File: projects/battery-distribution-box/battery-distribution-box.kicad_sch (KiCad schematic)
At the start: 6 parts, among them J1 Cells, J2 Diag, J3 Balancer, J4 Output, J5 Balancer enable

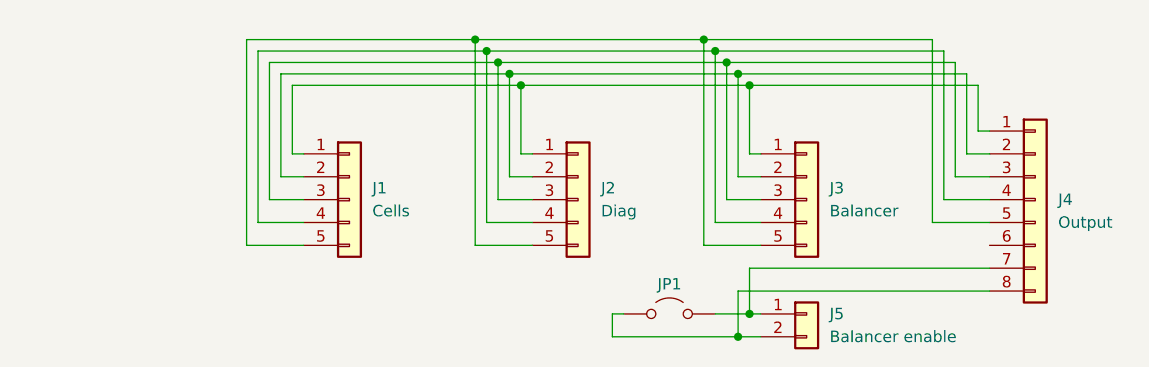
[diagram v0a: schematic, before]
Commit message: Moving to JST VH connectors. They are cheaper and easier to source.
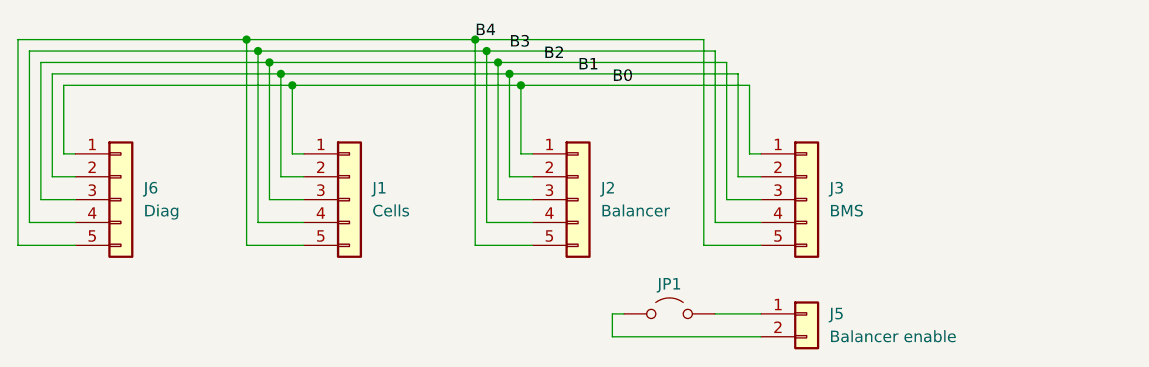
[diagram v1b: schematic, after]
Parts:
- removed J4: Output, Connector_RJ:RJ45_OST_PJ012-8P8CX_Vertical, symbol Connector_Generic:Conn_01x08
- added J6: Diag, Connector_JST:JST_VH_B5PS-VH_1x05_P3.96mm_Horizontal, symbol Connector_Generic:Conn_01x05
- J1: footprint Connector_Phoenix_MC:PhoenixContact_MCV_1,5_5-G-3.5_1x05_P3.50mm_Vertical -> Connector_JST:JST_VH_B5PS-VH_1x05_P3.96mm_Horizontal
- J2: value Diag -> Balancer; footprint Connector_Phoenix_MC:PhoenixContact_MCV_1,5_5-G-3.5_1x05_P3.50mm_Vertical -> Connector_JST:JST_VH_B5PS-VH_1x05_P3.96mm_Horizontal
- J3: value Balancer -> BMS; footprint Connector_Phoenix_MC:PhoenixContact_MCV_1,5_5-G-3.5_1x05_P3.50mm_Vertical -> Connector_JST:JST_VH_B5PS-VH_1x05_P3.96mm_Horizontal
- J5: footprint Connector_Phoenix_MC:PhoenixContact_MCV_1,5_2-G-3.5_1x02_P3.50mm_Vertical -> Connector_JST:JST_VH_B2PS-VH_1x02_P3.96mm_Horizontal
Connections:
- net B0: now reaches J1.1 (Pin_1), J2.1 (Pin_1), J3.1 (Pin_1)
- net B0: now also J6.1 (Pin_1)
- net B1: now reaches J1.2 (Pin_2), J2.2 (Pin_2), J3.2 (Pin_2)
- net B1: now also J6.2 (Pin_2)
- net B2: now reaches J1.3 (Pin_3), J2.3 (Pin_3), J3.3 (Pin_3)
- net B2: now also J6.3 (Pin_3)
- net B3: now reaches J1.4 (Pin_4), J2.4 (Pin_4), J3.4 (Pin_4)
- net B3: now also J6.4 (Pin_4)
- net B4: now reaches J1.5 (Pin_5), J2.5 (Pin_5), J3.5 (Pin_5)
- net B4: now also J6.5 (Pin_5)
